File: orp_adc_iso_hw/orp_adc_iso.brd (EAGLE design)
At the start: 39.4 x 56.8 mm, 25 parts, among them IC2 LM385MX-2.5_NOPB, IC3 ADS1115IDGSR, IC4 ADUM1250ARZ, J1 RF1-01B-D-00-75

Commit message: correct capacitor size used
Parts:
- removed C10: 100 uF, 293D106X9016B2TE3:CAPPM3528X210N
- added C11, C12, C13: 100 uF, rcl:SMC_C
- C7, C9: value 100 uF -> 100 nF; device 293D106X9016B2TE3:CAPPM3528X210N -> rcl:C0603
- moved C9 20.6 mm to (23.5, 21.1), turned to 180 degrees
- moved C7 15.6 mm to (28.0, 25.3), turned to 270 degrees
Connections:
- net GND: now also C13.-; no longer C10.2
- net GND_ISO: now also C11.-, C12.-
- net VCC5V: now also C13.+; no longer C10.1
- net VCC5V_ISO: now also C12.+; no longer C9.1
- net VREF2.5V: now also C11.+, C9.1
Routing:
- net GND_ISO: track 70.8 -> 46.3 mm, vias 11 -> 23
- net GND: track 25.3 -> 16.2 mm
- net N$4: track 4.59 -> 3.05 mm
- net VCC5V_ISO: track 79.7 -> 80.7 mm
- net VREF2.5V: track 64.7 -> 63.9 mm

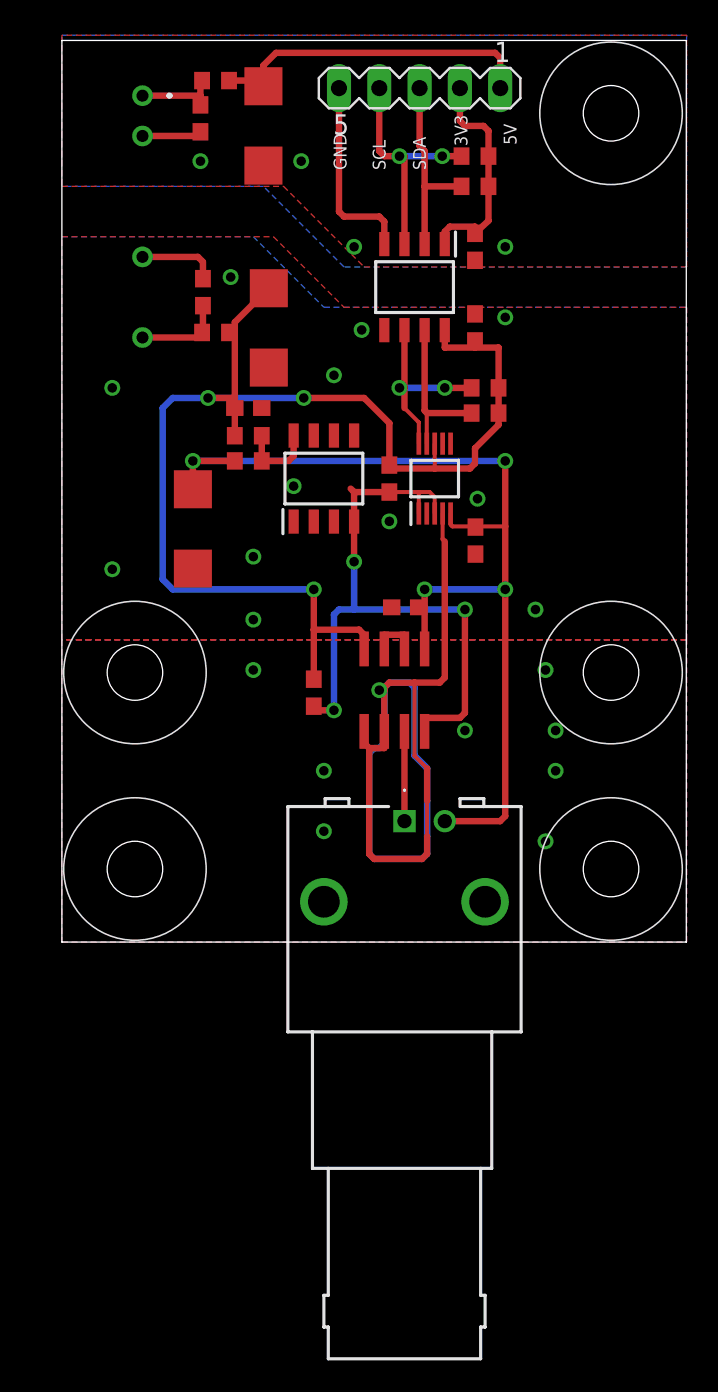
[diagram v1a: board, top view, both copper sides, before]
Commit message: improvement to displaying temp and orp when there is reading error
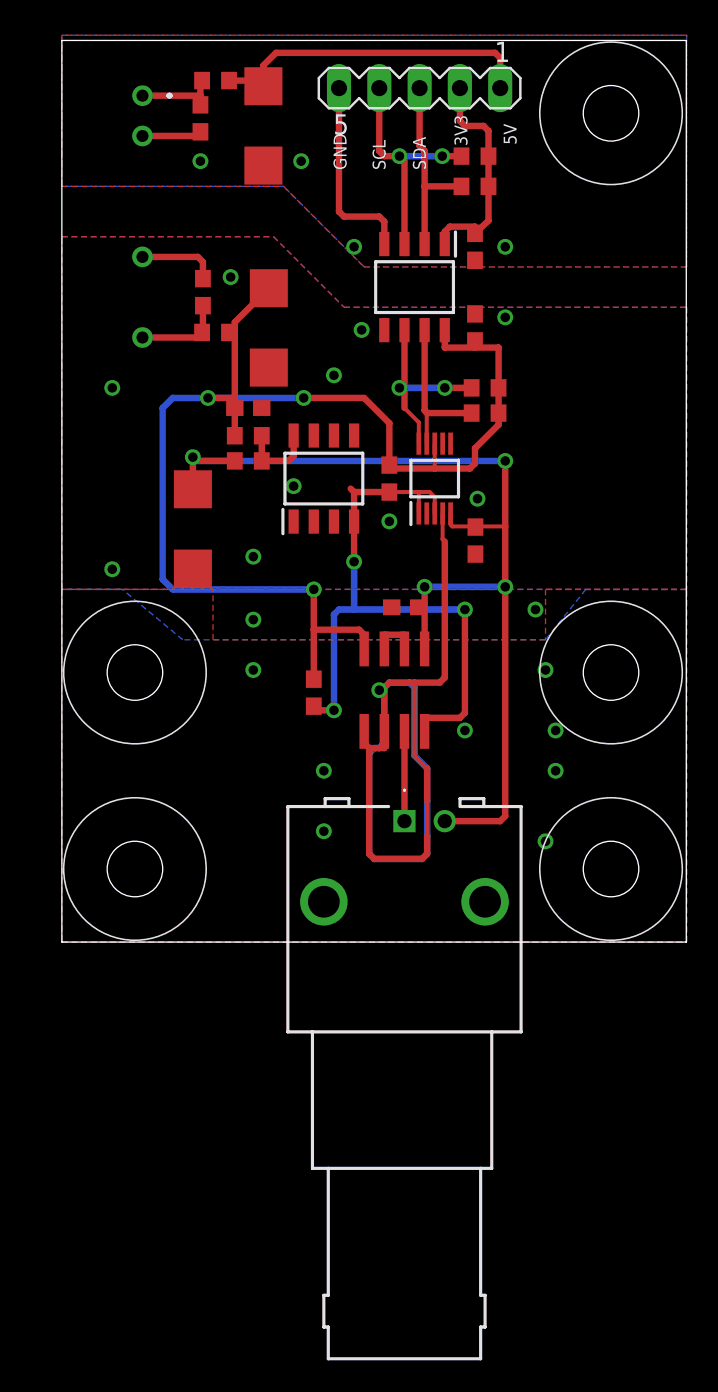
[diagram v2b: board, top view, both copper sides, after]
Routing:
- net VREF2.5V: track 63.9 -> 64.8 mm
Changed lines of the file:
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@@
 <layer number="23" name="tOrigins" color="15" fill="1" visible="yes" active="yes"/>
 <layer number="24" name="bOrigins" color="15" fill="1" visible="no" active="yes"/>
-<layer number="25" name="tNames" color="7" fill="1" visible="yes" active="yes"/>
+<layer number="25" name="tNames" color="7" fill="1" visible="no" active="yes"/>
 <layer number="26" name="bNames" color="7" fill="1" visible="no" active="yes"/>
-<layer number="27" name="tValues" color="7" fill="1" visible="yes" active="yes"/>
+<layer number="27" name="tValues" color="7" fill="1" visible="no" active="yes"/>
 <layer number="28" name="bValues" color="7" fill="1" visible="no" active="yes"/>
 <layer number="29" name="tStop" color="7" fill="3" visible="no" active="yes"/>
@@
 <contactref element="IC3" pad="5"/>
 <wire x1="12.8025" y1="30.32125" x2="10.16" y2="30.32125" width="0.4064" layer="1"/>
+<wire x1="10.16" y1="30.32125" x2="10.16" y2="30.559375" width="0.4064" layer="1"/>
 <wire x1="26.51125" y1="26.19375" x2="26.4" y2="26.305" width="0.254" layer="1"/>
 <wire x1="26.4" y1="26.305" x2="26.4" y2="27.01" width="0.254" layer="1"/>
-<via x="10.16" y="30.32125" extent="1-16" drill="0.6"/>
+<via x="10.16" y="30.559375" extent="1-16" drill="0.6"/>
+<wire x1="10.16" y1="30.559375" x2="10.16" y2="30.32125" width="0.4064" layer="16"/>
 <wire x1="10.16" y1="30.32125" x2="29.845" y2="30.32125" width="0.4064" layer="16"/>
 <via x="29.845" y="30.32125" extent="1-16" drill="0.6"/>
@@
 <wire x1="29.845" y1="26.19375" x2="27.94" y2="26.19375" width="0.254" layer="1"/>
 <wire x1="27.94" y1="26.19375" x2="26.51125" y2="26.19375" width="0.254" layer="1"/>
-<wire x1="29.845" y1="22.225" x2="29.845" y2="7.9375" width="0.4064" layer="1"/>
+<wire x1="29.845" y1="22.38375" x2="29.845" y2="7.9375" width="0.4064" layer="1"/>
 <wire x1="29.845" y1="7.9375" x2="29.5275" y2="7.62" width="0.4064" layer="1"/>
 <wire x1="29.5275" y1="7.62" x2="26.035" y2="7.62" width="0.4064" layer="1"/>
 <contactref element="U$1" pad="5"/>
-<wire x1="29.845" y1="22.225" x2="29.845" y2="26.19375" width="0.4064" layer="1"/>
+<wire x1="29.845" y1="22.38375" x2="29.845" y2="26.19375" width="0.4064" layer="1"/>
 <wire x1="24.765" y1="18.475" x2="24.765" y2="21.095625" width="0.4064" layer="1"/>
-<via x="24.765" y="22.225" extent="1-16" drill="0.6"/>
-<wire x1="24.765" y1="21.095625" x2="24.765" y2="22.225" width="0.4064" layer="1"/>
-<wire x1="24.765" y1="22.225" x2="29.845" y2="22.225" width="0.4064" layer="16"/>
-<via x="29.845" y="22.225" extent="1-16" drill="0.6"/>
+<via x="24.765" y="22.38375" extent="1-16" drill="0.6"/>
+<wire x1="24.765" y1="21.095625" x2="24.765" y2="22.38375" width="0.4064" layer="1"/>
+<wire x1="24.765" y1="22.38375" x2="29.845" y2="22.38375" width="0.4064" layer="16"/>
+<via x="29.845" y="22.38375" extent="1-16" drill="0.6"/>
 <contactref element="C11" pad="+"/>
-<wire x1="10.16" y1="30.32125" x2="10.16" y2="28.535" width="0.4064" layer="1"/>
+<wire x1="10.16" y1="30.559375" x2="10.16" y2="28.535" width="0.4064" layer="1"/>
 <contactref element="C7" pad="1"/>
 <contactref element="C9" pad="1"/>
@@
 <vertex x="41.275" y="57.15"/>
 <vertex x="41.275" y="42.545"/>
-<vertex x="19.685" y="42.545"/>
-<vertex x="14.605" y="47.625"/>
+<vertex x="20.955" y="42.545"/>
+<vertex x="15.875" y="47.625"/>
 </polygon>
 <via x="29.845" y="43.815" extent="1-16" drill="0.6"/>
@@
 <wire x1="24.4" y1="27.01" x2="24.4" y2="28.36" width="0.254" layer="1"/>
 <polygon width="0.254" layer="16" isolate="0.4064">
-<vertex x="1.905" y="19.05"/>
+<vertex x="1.905" y="22.225"/>
 <vertex x="1.905" y="44.45"/>
-<vertex x="13.97" y="44.45"/>
-<vertex x="18.415" y="40.005"/>
+<vertex x="15.24" y="44.45"/>
+<vertex x="19.685" y="40.005"/>
 <vertex x="41.275" y="40.005"/>
-<vertex x="41.275" y="19.05"/>
+<vertex x="41.275" y="22.225"/>
+<vertex x="34.925" y="22.225"/>
+<vertex x="32.385" y="19.05"/>
+<vertex x="9.525" y="19.05"/>
+<vertex x="5.715" y="22.225"/>
 </polygon>
 <polygon width="0.254" layer="1" isolate="0.4064" rank="2">
@@
 <vertex x="19.685" y="40.005"/>
 <vertex x="41.275" y="40.005"/>
-<vertex x="41.275" y="19.05"/>
-<vertex x="1.905" y="19.05"/>
+<vertex x="41.275" y="22.225"/>
+<vertex x="32.385" y="22.225"/>
+<vertex x="32.385" y="19.05"/>
+<vertex x="11.43" y="19.05"/>
+<vertex x="11.43" y="22.225"/>
+<vertex x="1.905" y="22.225"/>
 </polygon>
 <via x="29.845" y="39.37" extent="1-16" drill="0.6"/>
@@
 <wire x1="20.32" y1="23.97125" x2="20.32" y2="20.955" width="0.4064" layer="16"/>
 <polygon width="0.254" layer="1" isolate="1.6764" orphans="yes">
-<vertex x="1.905" y="19.05"/>
+<vertex x="1.905" y="22.225"/>
 <vertex x="1.905" y="0"/>
 <vertex x="41.275" y="0"/>
-<vertex x="41.275" y="19.05"/>
+<vertex x="41.275" y="22.225"/>
 </polygon>
 <polygon width="0.254" layer="16" isolate="1.6764" orphans="yes">
-<vertex x="1.905" y="19.05"/>
+<vertex x="1.905" y="22.225"/>
 <vertex x="1.905" y="0"/>
 <vertex x="41.275" y="0"/>
-<vertex x="41.275" y="19.05"/>
+<vertex x="41.275" y="22.225"/>
 </polygon>
 <contactref element="C11" pad="-"/>

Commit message: orp module added on thermostat base board
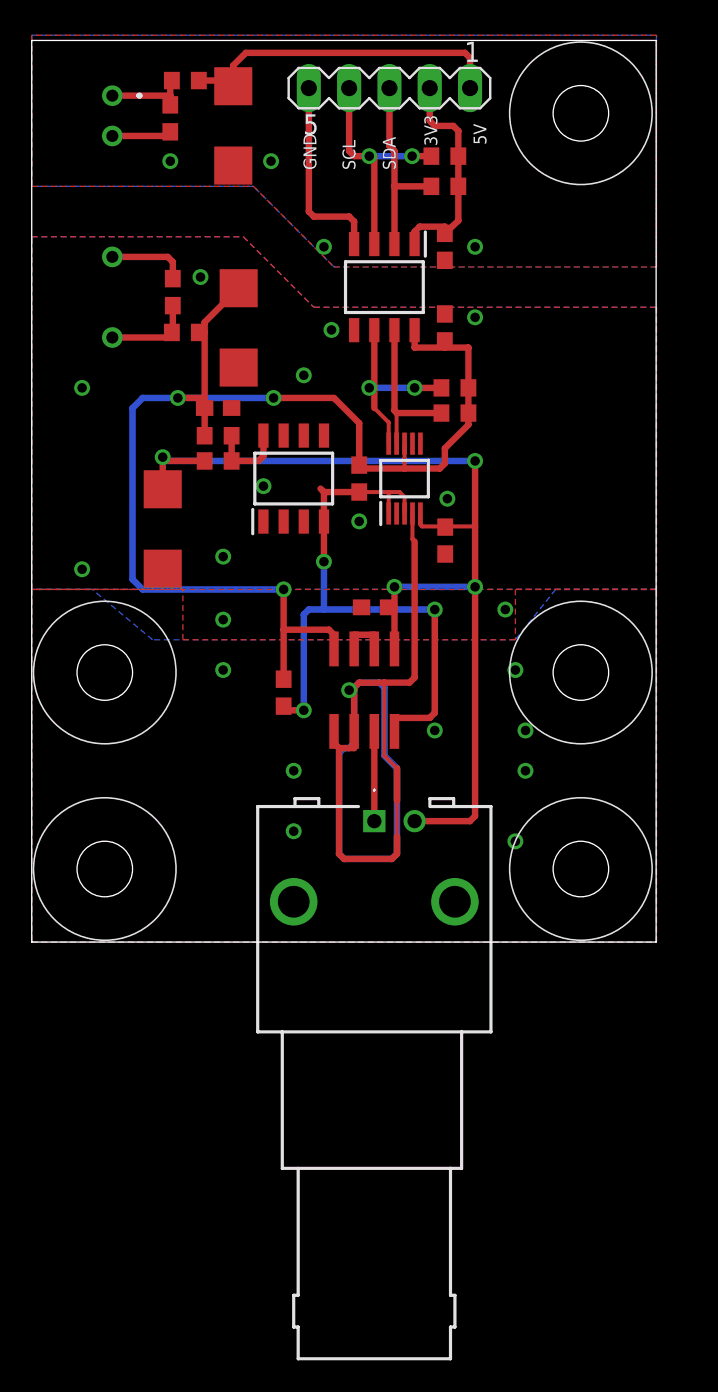
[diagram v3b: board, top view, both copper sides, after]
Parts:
- moved C3 1.90 mm to (20.6, 29.2)
- moved C4 1.90 mm to (26.0, 38.7)
- moved C5 1.90 mm to (26.0, 43.8)
- moved J1 1.90 mm to (21.6, 7.62)
- moved R4 1.90 mm to (26.0, 47.6)
- moved R5 1.90 mm to (26.0, 49.5)
- moved SV1 1.90 mm to (22.5, 53.8)
- moved C1 1.90 mm to (15.9, 15.7)
- moved C11 1.90 mm to (8.26, 26.0)
- moved C12 1.90 mm to (13.0, 38.7)
- moved C13 1.90 mm to (12.7, 51.4)
- moved C2 1.90 mm to (11.8, 33.7)
- moved C6 1.90 mm to (8.89, 41.0)
- moved C8 1.90 mm to (8.74, 51.9)
- moved PS1 1.90 mm to (5.08, 53.3)
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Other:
- board size 39.4 x 56.8 mm -> 39.3 x 56.8 mm

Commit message: orp board made bigger to have whole bnc connector on pcb
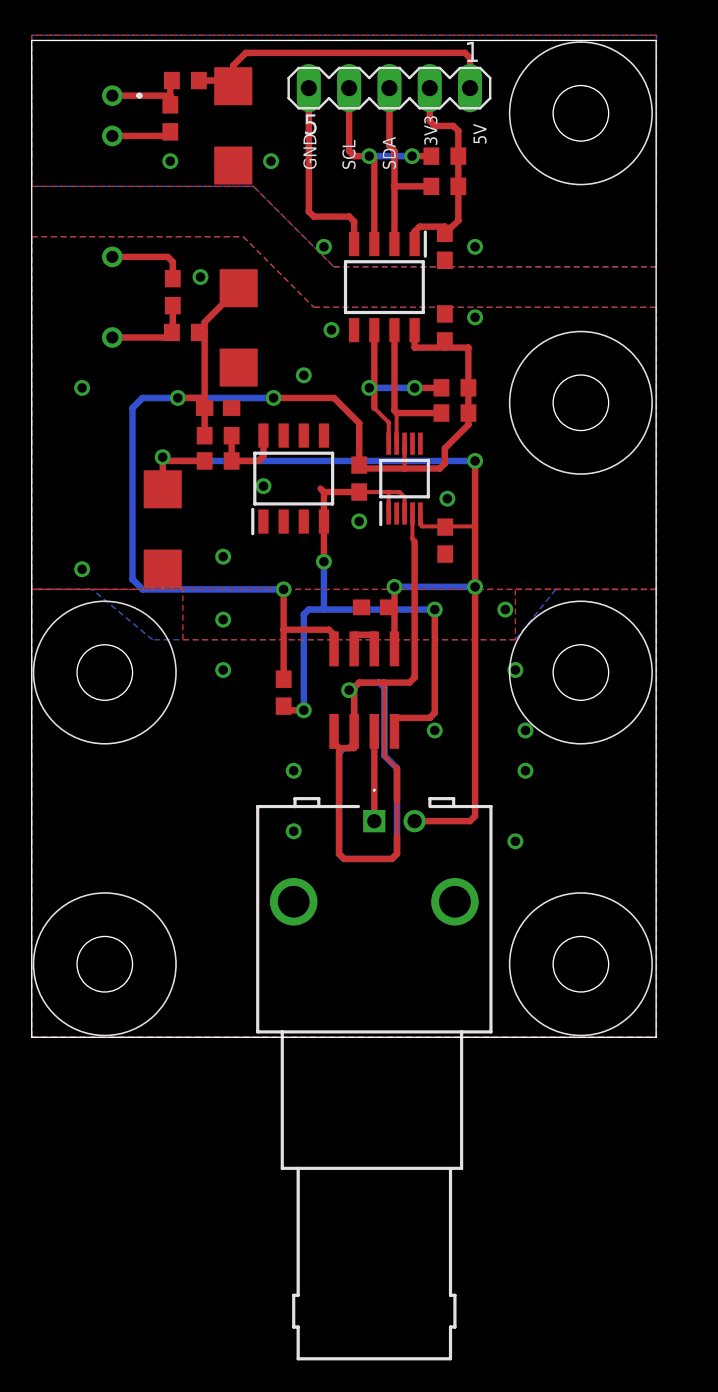
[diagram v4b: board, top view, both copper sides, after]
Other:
- board size 39.3 x 56.8 mm -> 39.3 x 62.8 mm
